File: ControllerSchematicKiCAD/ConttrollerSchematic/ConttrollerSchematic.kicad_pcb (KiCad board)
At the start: 2 copper layers, 175 x 50 mm, 10 parts, among them SW1 SW_Push, SW2 SW_Push

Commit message: Schematic updates
lots of stuff
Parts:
- removed D1, D2, D3, D4: LED, LED_THT:LED_D5.0mm
- removed REF** (x2): PinSocket_1x15_P2.54mm_Vertical, Connector_PinSocket_2.54mm:PinSocket_1x15_P2.54mm_Vertical
- removed REF**: PinSocket_1x05_P2.54mm_Horizontal, Connector_PinSocket_2.54mm:PinSocket_1x05_P2.54mm_Horizontal
- removed REF**: Buzzer_12x9.5RM7.6, Buzzer_Beeper:Buzzer_12x9.5RM7.6
- removed SW1, SW2: SW_Push, Button_Switch_SMD:SW_Push_1P1T-SH_NO_CK_KMR2xxG
- added Button1: SW_Push, Button_Switch_SMD:SW_Push_1P1T-SH_NO_CK_KMR2xxG, F.Cu at (197.6, 136.6)
- added Button2: SW_Push, Button_Switch_SMD:SW_Push_1P1T-SH_NO_CK_KMR2xxG, F.Cu at (188.5, 137.3)
- added Joystick1: Conn_01x05_Socket, Connector_PinSocket_2.54mm:PinSocket_1x05_P2.54mm_Horizontal, F.Cu at (108.8, 129.8)
- added LED1: LED, LED_THT:LED_D5.0mm, F.Cu at (191.6, 121.7)
- added LED2: LED, LED_THT:LED_D5.0mm, F.Cu at (181.1, 121.7)
- added LeftESP1: Conn_01x15_Pin, Connector_PinSocket_2.54mm:PinSocket_1x15_P2.54mm_Vertical, F.Cu at (142.7, 117.8)
- added RightESP1: Conn_01x15_Pin, Connector_PinSocket_2.54mm:PinSocket_1x15_P2.54mm_Vertical, F.Cu at (159.2, 117.7)
- added Screen1: Conn_01x04_Socket, Connector_PinSocket_1.00mm:PinSocket_1x04_P1.00mm_Vertical, F.Cu at (99.0, 120.1)

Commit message: auto routed
heheh
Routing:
- net GND: track 0.00 -> 154.3 mm, vias 0 -> 1
- net Net-(RightESP1-Pin_14): track 0.00 -> 105.5 mm, vias 0 -> 1
- net Net-(RightESP1-Pin_11): track 0.00 -> 86.1 mm, vias 0 -> 1
- net V+: track 0.00 -> 85.6 mm
- net Net-(LeftESP1-Pin_3): track 0.00 -> 76.3 mm, vias 0 -> 1
- net Net-(LED1-A): track 0.00 -> 67.9 mm, vias 0 -> 1
- net Net-(LED2-A): track 0.00 -> 65.2 mm, vias 0 -> 1
- net Net-(LeftESP1-Pin_6): track 0.00 -> 55.2 mm
- net /L8: track 0.00 -> 39.2 mm
- net /Pin L5: track 0.00 -> 34.7 mm
- net /L7: track 0.00 -> 34.7 mm

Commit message: moved something
moved the esp
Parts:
- moved RightESP1 1.78 mm to (161.0, 117.7)
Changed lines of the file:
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@@
 	(footprint "Connector_PinSocket_2.54mm:PinSocket_1x15_P2.54mm_Vertical"
 		(layer "F.Cu")
-		(at 159.22 117.73)
+		(at 161 117.73)
 		(descr "Through hole straight socket strip, 1x15, 2.54mm pitch, single row (from Kicad 4.0.7), script generated")
 		(tags "Through hole socket strip THT 1x15 2.54mm single row")
@@
 	)
 	(segment
-		(start 159.22 117.73)
-		(end 160.3717 117.73)
-		(width 0.2)
-		(layer "F.Cu")
-		(net 1)
-	)
-	(segment
-		(start 164.3517 121.71)
-		(end 181.08 121.71)
+		(start 161 117.73)
+		(end 162.1517 117.73)
+		(width 0.2)
+		(layer "F.Cu")
+		(net 1)
+	)
+	(segment
+		(start 166.1317 121.71)
+		(end 182.86 121.71)
 		(width 0.2)
 		(layer "F.Cu")
@@
 	)
 	(segment
-		(start 142.68 119.525)
-		(end 156.2733 119.525)
+		(start 144.46 119.525)
+		(end 158.0533 119.525)
 		(width 0.2)
 		(layer "F.Cu")
@@
 	)
 	(segment
-		(start 160.3717 117.73)
-		(end 164.3517 121.71)
+		(start 162.1517 117.73)
+		(end 166.1317 121.71)
 		(width 0.2)
 		(layer "F.Cu")
@@
 	)
 	(segment
-		(start 159.22 117.73)
-		(end 158.0683 117.73)
+		(start 161 117.73)
+		(end 159.8483 117.73)
 		(width 0.2)
 		(layer "F.Cu")
@@
 	)
 	(segment
-		(start 156.2733 119.525)
-		(end 158.0683 117.73)
+		(start 158.0533 119.525)
+		(end 159.8483 117.73)
 		(width 0.2)
 		(layer "F.Cu")
@@
 	)
 	(segment
-		(start 157.9825 121.5075)
-		(end 159.22 120.27)
+		(start 159.7625 121.5075)
+		(end 161 120.27)
 		(width 0.2)
 		(layer "F.Cu")
@@
 	)
 	(segment
-		(start 138.2257 121.5075)
-		(end 157.9825 121.5075)
+		(start 140.0057 121.5075)
+		(end 159.7625 121.5075)
 		(width 0.2)
 		(layer "F.Cu")
@@
 	)
 	(segment
-		(start 145.8122 139.2417)
-		(end 192.9666 139.2417)
+		(start 147.5922 139.2417)
+		(end 194.7466 139.2417)
 		(width 0.2)
 		(layer "F.Cu")
@@
 	)
 	(segment
-		(start 165.179 137.3002)
-		(end 159.6971 131.8183)
+		(start 166.959 137.3002)
+		(end 161.4771 131.8183)
 		(width 0.2)
 		(layer "F.Cu")
@@
 	)
 	(segment
-		(start 158.2933 134.24)
-		(end 146.44 134.24)
+		(start 160.0733 134.24)
+		(end 148.22 134.24)
 		(width 0.2)
 		(layer "F.Cu")
@@
 	)
 	(segment
-		(start 158.743 131.8183)
-		(end 158.0683 132.493)
+		(start 160.523 131.8183)
+		(end 159.8483 132.493)
 		(width 0.2)
 		(layer "F.Cu")
@@
 	)
 	(segment
-		(start 158.3413 134.192)
-		(end 158.2933 134.24)
-		(width 0.2)
-		(layer "F.Cu")
-		(net 7)
-	)
-	(segment
-		(start 158.3413 134.192)
-		(end 158.2933 134.24)
-		(width 0.2)
-		(layer "F.Cu")
-		(net 7)
-	)
-	(segment
-		(start 158.0683 133.919)
-		(end 158.3413 134.192)
-		(width 0.2)
-		(layer "F.Cu")
-		(net 7)
-	)
-	(segment
-		(start 159.6971 131.8183)
-		(end 158.743 131.8183)
-		(width 0.2)
-		(layer "F.Cu")
-		(net 7)
-	)
-	(segment
-		(start 158.0683 132.493)
-		(end 158.0683 133.919)
+		(start 160.1213 134.192)
+		(end 160.0733 134.24)
+		(width 0.2)
+		(layer "F.Cu")
+		(net 7)
+	)
+	(segment
+		(start 160.1213 134.192)
+		(end 160.0733 134.24)
+		(width 0.2)
+		(layer "F.Cu")
+		(net 7)
+	)
+	(segment
+		(start 159.8483 133.919)
+		(end 160.1213 134.192)
+		(width 0.2)
+		(layer "F.Cu")
+		(net 7)
+	)
+	(segment
+		(start 161.4771 131.8183)
+		(end 160.523 131.8183)
+		(width 0.2)
+		(layer "F.Cu")
+		(net 7)
+	)
+	(segment
+		(start 159.8483 132.493)
+		(end 159.8483 133.919)
 		(width 0.2)
 		(layer "F.Cu")
@@
 	)
 	(segment
-		(start 145.3716 126.7205)
-		(end 189.1295 126.7205)
+		(start 147.1516 126.7205)
+		(end 190.9095 126.7205)
 		(width 0.2)
 		(layer "F.Cu")
@@
 	)
 	(segment
-		(start 146.5713 124.08)
-		(end 181.25 124.08)
+		(start 148.3513 124.08)
+		(end 183.03 124.08)
 		(width 0.2)
 		(layer "F.Cu")
@@
 	)
 	(segment
-		(start 158 149.53)
-		(end 159.22 150.75)
+		(start 159.78 149.53)
+		(end 161 150.75)
 		(width 0.2)
 		(layer "F.Cu")
@@
 	)
 	(segment
-		(start 102.2056 149.53)
-		(end 158 149.53)
+		(start 103.9856 149.53)
+		(end 159.78 149.53)
 		(width 0.2)
 		(layer "F.Cu")
@@
 	)
 	(segment
-		(start 159.22 143.13)
-		(end 158.0763 141.9863)
+		(start 161 143.13)
+		(end 159.8563 141.9863)
 		(width 0.2)
 		(layer "F.Cu")
@@
 	)
 	(segment
-		(start 158.0763 141.9863)
-		(end 103.5375 141.9863)
-		(width 0.2)
-		(layer "F.Cu")
+		(start 159.8563 141.9863)
+		(end 105.3175 141.9863)
+		(width 0.2)
+		(layer "F.Cu")

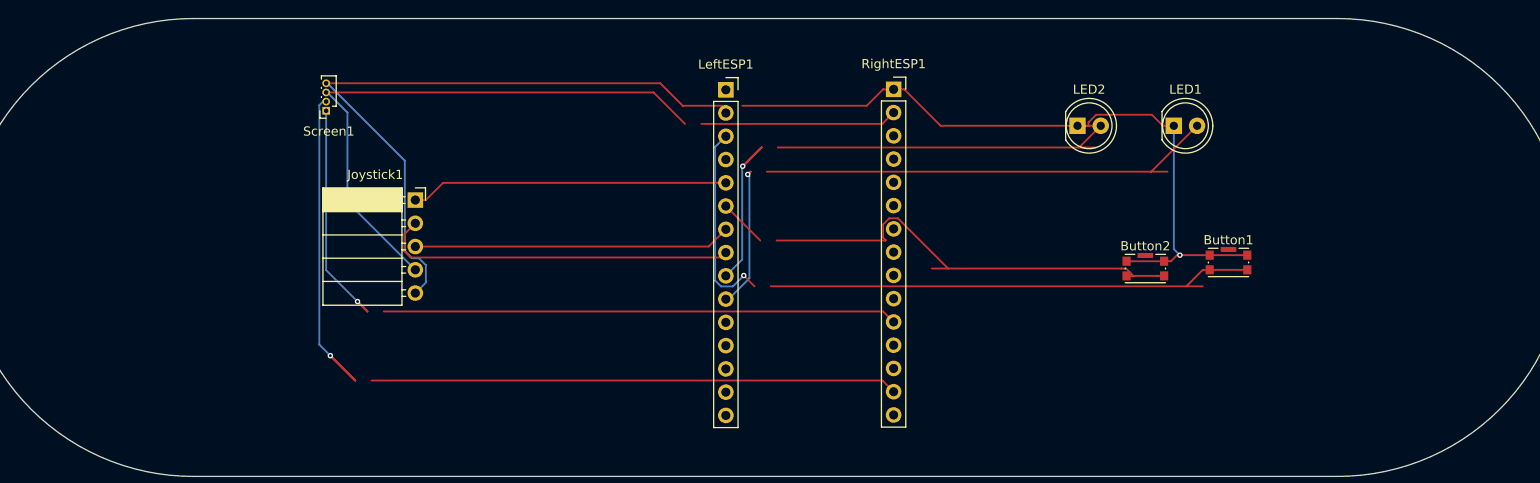
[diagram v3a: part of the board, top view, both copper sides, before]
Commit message: I changed the location of some stuff redo the button size
Changed buttons footprint, delete all wiring for now
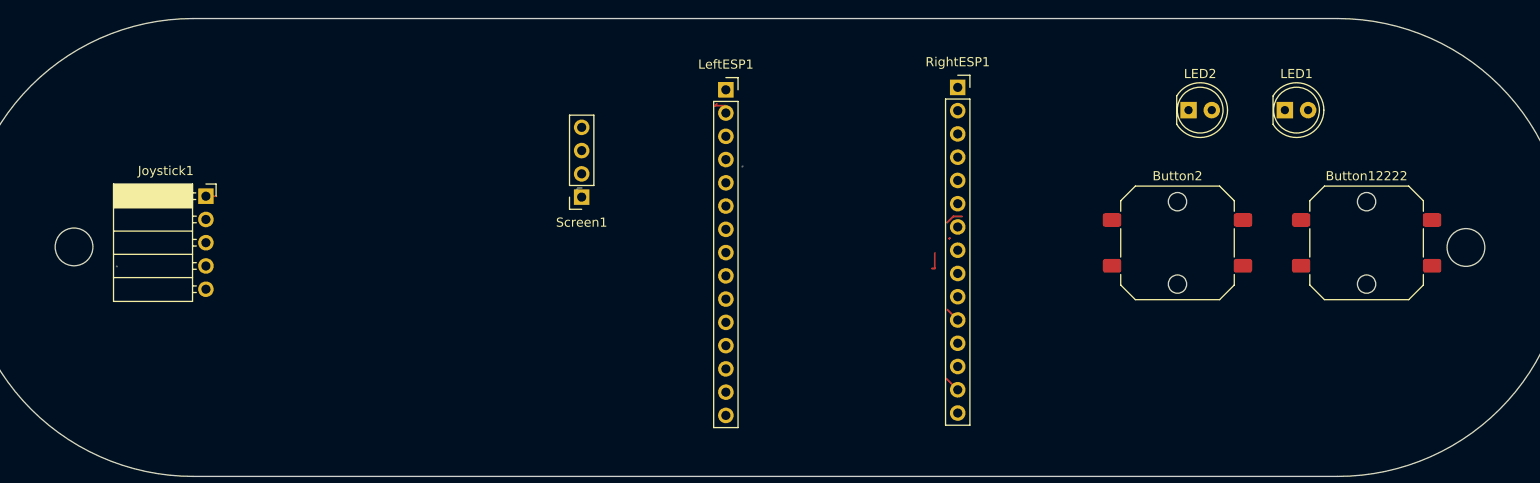
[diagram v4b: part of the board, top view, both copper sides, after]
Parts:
- Button12222: renamed from Button1; footprint Button_Switch_SMD:SW_Push_1P1T-SH_NO_CK_KMR2xxG -> Button_Switch_SMD:SW_Push_1P1T_NO_CK_PTS125Sx73PSMTR
- Button2: footprint Button_Switch_SMD:SW_Push_1P1T-SH_NO_CK_KMR2xxG -> Button_Switch_SMD:SW_Push_1P1T_NO_CK_PTS125Sx73PSMTR
- Screen1: footprint Connector_PinSocket_1.00mm:PinSocket_1x04_P1.00mm_Vertical -> Connector_PinSocket_2.54mm:PinSocket_1x04_P2.54mm_Vertical
- moved Screen1 29.5 mm to (126.9, 129.5)
- moved Joystick1 22.9 mm to (85.9, 129.4)
- moved Button12222 15.2 mm to (212.7, 134.5)
- moved LED1 12.2 mm to (203.7, 120.0)
- moved LED2 12.2 mm to (193.2, 120.0)
- moved RightESP1 7.00 mm to (168.0, 117.5)
- moved Button2 4.49 mm to (192.0, 134.5)
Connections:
- net /Pin L5 renamed /L5
- net Net-(LED1-A) renamed /L10
- net Net-(LED2-A) renamed /L9
- net Net-(LeftESP1-Pin_3) renamed /L3
- net Net-(LeftESP1-Pin_6) renamed /L6
- net Net-(RightESP1-Pin_11) renamed /R14
- net Net-(RightESP1-Pin_14) renamed /R11
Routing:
- net GND: track 154.3 -> 2.27 mm, vias 1 -> 0
- net /R11: track 105.5 -> 1.99 mm, vias 1 -> 0
- net V+: track 85.6 -> 0.00 mm
- net /R14: track 86.1 -> 2.55 mm, vias 1 -> 0
- net /L3: track 76.3 -> 0.00 mm, vias 1 -> 0
- net /L10: track 67.9 -> 0.30 mm, vias 1 -> 0
- net /L9: track 65.2 -> 0.08 mm, vias 1 -> 0
- net /L6: track 55.2 -> 0.00 mm
- net /L8: track 39.2 -> 0.75 mm
- net /L7: track 34.7 -> 0.00 mm
- net /L5: track 34.7 -> 1.15 mm
- net unconnected-(RightESP1-Pin_9-Pad9): track 0.00 -> 4.06 mm
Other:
- outline, holes or cut-outs redrawn

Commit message: changed the dimension
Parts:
- moved LeftESP1 76.1 mm to (141.5, 41.7)
- moved RightESP1 76.1 mm to (166.8, 41.5)
- moved Button2 75.7 mm to (197.8, 59.0)
- moved LED1 75.7 mm to (209.6, 44.5)
- moved LED2 75.7 mm to (199.1, 44.5)
- moved Button12222 75.6 mm to (216.8, 59.0)
- moved Joystick1 75.6 mm to (88.9, 53.9)
- moved Screen1 69.2 mm to (125.0, 60.3)
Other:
- board size 175 x 50 mm -> 174 x 42 mm
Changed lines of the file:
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@@
 	(footprint "Connector_PinSocket_2.54mm:PinSocket_1x05_P2.54mm_Horizontal"
 		(layer "F.Cu")
-		(at 85.9 129.4)
+		(at 88.9 53.9)
 		(descr "Through hole angled socket strip, 1x05, 2.54mm pitch, 8.51mm socket length, single row (from Kicad 4.0.7), script generated")
 		(tags "Through hole angled socket strip THT 1x05 2.54mm single row")
@@
 	(footprint "Connector_PinSocket_2.54mm:PinSocket_1x15_P2.54mm_Vertical"
 		(layer "F.Cu")
-		(at 142.68 117.78)
+		(at 141.5 41.72)
 		(descr "Through hole straight socket strip, 1x15, 2.54mm pitch, single row (from Kicad 4.0.7), script generated")
 		(tags "Through hole socket strip THT 1x15 2.54mm single row")
@@
 	(footprint "LED_THT:LED_D5.0mm"
 		(layer "F.Cu")
-		(at 203.725 120)
+		(at 209.575 44.5)
 		(descr "LED, diameter 5.0mm, 2 pins, http://cdn-reichelt.de/documents/datenblatt/A500/LL-504BC2E-009.pdf, generated by kicad-footprint-generator")
 		(tags "LED")
@@
 	(footprint "Button_Switch_SMD:SW_Push_1P1T_NO_CK_PTS125Sx73PSMTR"
 		(layer "F.Cu")
-		(at 192 134.5)
+		(at 197.85 59)
 		(descr "Tactile switch, 12x12 mm, H7.3 mm, square snap fit actuator, with pegs, gullwing terminals, https://www.ckswitches.com/media/1462/pts125.pdf")
 		(tags "button tactile switch SPST 1P1T C&K")
@@
 	(footprint "Button_Switch_SMD:SW_Push_1P1T_NO_CK_PTS125Sx73PSMTR"
 		(layer "F.Cu")
-		(at 212.65 134.5)
+		(at 216.85 59)
 		(descr "Tactile switch, 12x12 mm, H7.3 mm, square snap fit actuator, with pegs, gullwing terminals, https://www.ckswitches.com/media/1462/pts125.pdf")
 		(tags "button tactile switch SPST 1P1T C&K")
@@
 	(footprint "LED_THT:LED_D5.0mm"
 		(layer "F.Cu")
-		(at 193.205 120)
+		(at 199.055 44.5)
 		(descr "LED, diameter 5.0mm, 2 pins, http://cdn-reichelt.de/documents/datenblatt/A500/LL-504BC2E-009.pdf, generated by kicad-footprint-generator")
 		(tags "LED")
@@
 	(footprint "Connector_PinSocket_2.54mm:PinSocket_1x04_P2.54mm_Vertical"
 		(layer "F.Cu")
-		(at 126.93575 129.5 180)
+		(at 124.975 60.3 180)
 		(descr "Through hole straight socket strip, 1x04, 2.54mm pitch, single row (from Kicad 4.0.7), script generated")
 		(tags "Through hole socket strip THT 1x04 2.54mm single row")
 		(property "Reference" "Screen1"
-			(at 0 -2.77 180)
+			(at 1.18 73.29 180)
 			(layer "F.SilkS")
 			(effects
@@
 	(footprint "Connector_PinSocket_2.54mm:PinSocket_1x15_P2.54mm_Vertical"
 		(layer "F.Cu")
-		(at 168 117.52)
+		(at 166.82 41.46)
 		(descr "Through hole straight socket strip, 1x15, 2.54mm pitch, single row (from Kicad 4.0.7), script generated")
 		(tags "Through hole socket strip THT 1x15 2.54mm single row")
@@
 	)
 	(gr_circle
-		(center 71.5 134.938447)
-		(end 71 136.938447)
+		(center 69.5 59)
+		(end 69 61)
 		(stroke
 			(width 0.05)
@@
 	)
 	(gr_arc
-		(start 84.5 160)
-		(mid 59.5 135)
-		(end 84.5 110)
+		(start 86.49226 79.918734)
+		(mid 63.495832 59.622458)
+		(end 85.25 38)
 		(stroke
 			(width 0.05)
@@
 		(layer "Edge.Cuts")
 	)
-	(gr_circle
-		(center 223.5 135)
-		(end 223 137)
+	(gr_arc
+		(start 216.509235 38)
+		(mid 237.5 58.37728)
+		(end 217.754128 79.963069)
 		(stroke
 			(width 0.05)
 			(type default)
 		)
-		(fill no)
 		(layer "Edge.Cuts")
 	)
-	(gr_line
-		(start 209.5 160)
-		(end 84.5 160)
+	(gr_circle
+		(center 232 58.5)
+		(end 231.5 60.5)
 		(stroke
 			(width 0.05)
 			(type default)
 		)
+		(fill no)
 		(layer "Edge.Cuts")
 	)
-	(gr_arc
-		(start 209.5 110)
-		(mid 234.5 135)
-		(end 209.5 160)
+	(gr_line
+		(start 218 79.918734)
+		(end 86 79.918734)
 		(stroke
 			(width 0.05)
-			(type default)
+			(type solid)
 		)
 		(layer "Edge.Cuts")
 	)
 	(gr_line
-		(start 84.5 110)
-		(end 209.5 110)
+		(start 85.25 38)
+		(end 217.25 38)
 		(stroke
 			(width 0.05)
-			(type default)
+			(type solid)
 		)
 		(layer "Edge.Cuts")
 	)
 	(segment
-		(start 141.71 119.315)
-		(end 141.5 119.525)
+		(start 140.53 43.255)
+		(end 140.32 43.465)
 		(width 0.2)
 		(layer "F.Cu")
@@
 	)
 	(segment
-		(start 142.68 119.525)
-		(end 141.5 119.525)
+		(start 141.5 43.465)
+		(end 140.32 43.465)
 		(width 0.2)
 		(layer "F.Cu")
@@
 	)
 	(segment
-		(start 142.68 120.32)
-		(end 142.68 119.525)
+		(start 141.5 44.26)
+		(end 141.5 43.465)
 		(width 0.2)
 		(layer "F.Cu")
@@
 	)
 	(segment
-		(start 142.1463 136.0937)
-		(end 142.68 135.56)
+		(start 140.9663 60.0337)
+		(end 141.5 59.5)
 		(width 0.2)
 		(layer "F.Cu")
@@
 	)
 	(segment
-		(start 85.9 129.4)
-		(end 87.0517 129.4)
+		(start 88.9 53.9)
+		(end 90.0517 53.9)
 		(width 0.2)
 		(layer "F.Cu")
@@
 	)
 	(segment
-		(start 142.68 140.64)
-		(end 142.9798 140.64)
+		(start 141.5 64.58)
+		(end 141.7998 64.58)
 		(width 0.2)
 		(layer "B.Cu")
@@
 	)
 	(segment
-		(start 144.525 126.1263)
-		(end 144.4688 126.1825)
+		(start 143.345 50.0663)
+		(end 143.2888 50.1225)
 		(width 0.2)
 		(layer "B.Cu")
@@
 	)
 	(segment
-		(start 167.1033 134)
-		(end 167.0733 134.03)
+		(start 165.9233 57.94)
+		(end 165.8933 57.97)
 		(width 0.2)
 		(layer "F.Cu")
@@
 	)
 	(segment
-		(start 165.5 137.3002)
-		(end 165.179 137.3002)
+		(start 164.32 61.2402)
+		(end 163.999 61.2402)
 		(width 0.2)
 		(layer "F.Cu")
@@
 	)
 	(segment
-		(start 167.523 131.6083)
-		(end 166.8483 132.283)
+		(start 166.343 55.5483)
+		(end 165.6683 56.223)
 		(width 0.2)
 		(layer "F.Cu")
@@
 	)
 	(segment
-		(start 165.5 135.6033)
-		(end 165.5 137.3002)
+		(start 164.32 59.5433)
+		(end 164.32 61.2402)
 		(width 0.2)
 		(layer "F.Cu")
@@
 	)
 	(segment
-		(start 167.1213 133.982)
-		(end 167.1033 134)
+		(start 165.9413 57.922)
+		(end 165.9233 57.94)
 		(width 0.2)
 		(layer "F.Cu")
@@
 	)
 	(segment
-		(start 167.1213 133.982)
-		(end 167.0733 134.03)
+		(start 165.9413 57.922)
+		(end 165.8933 57.97)
 		(width 0.2)
 		(layer "F.Cu")
@@
 	)
 	(segment
-		(start 168.4771 131.6083)
-		(end 167.523 131.6083)
+		(start 167.2971 55.5483)
+		(end 166.343 55.5483)
 		(width 0.2)
 		(layer "F.Cu")
@@
 	)
 	(segment
-		(start 126.93575 126.5)
-		(end 127.07595 126.5)
+		(start 124.975 57.3)
+		(end 125.1152 57.3)
 		(width 0.2)
 		(layer "B.Cu")
@@
 	)
 	(segment
-		(start 126.93575 127.5)
-		(end 127.06425 127.5)
+		(start 124.975 58.3)
+		(end 125.1035 58.3)
 		(width 0.2)
 		(layer "B.Cu")
@@
 	)
 	(segment
-		(start 168 142.92)
-		(end 166.8563 141.7763)
+		(start 166.82 66.86)
+		(end 165.6763 65.7163)
 		(width 0.2)
 		(layer "F.Cu")
@@
 		(width 0.2)
 		(layer "B.Cu")
-		(net 29)
-	)
-	(segment
-		(start 76.1812 137.08)
-		(end 76.16 137.0588)
-		(width 0.2)
-		(layer "B.Cu")

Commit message: something more
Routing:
- net unconnected-(RightESP1-Pin_9-Pad9): track 4.06 -> 0.00 mm
- net /R14: track 2.52 -> 0.00 mm
- net GND: track 2.27 -> 0.00 mm
- net /R11: track 1.99 -> 0.00 mm
- net /L5: track 1.15 -> 0.00 mm
- net /L8: track 0.75 -> 0.00 mm
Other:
- outline, holes or cut-outs redrawn
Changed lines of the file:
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@@
 			(at 1.18 73.29 180)
 			(layer "F.SilkS")
+			(hide yes)
 			(effects
 				(font
@@
 		(layer "Edge.Cuts")
 	)
+	(gr_line
+		(start 85.999997 79.959574)
+		(end 86 79.918734)
+		(stroke
+			(width 0.05)
+			(type default)
+		)
+		(layer "Edge.Cuts")
+	)
 	(gr_arc
-		(start 86.49226 79.918734)
-		(mid 63.495832 59.622458)
-		(end 85.25 38)
+		(start 86 79.959574)
+		(mid 63.490176 59.375542)
+		(end 85.249993 38.000208)
 		(stroke
 			(width 0.05)
@@
 	)
 	(gr_arc
-		(start 216.509235 38)
-		(mid 237.5 58.37728)
-		(end 217.754128 79.963069)
+		(start 217.25 38)
+		(mid 237.518909 58.623)
+		(end 218.002934 79.959904)
 		(stroke
 			(width 0.05)
@@
 		(layer "Edge.Cuts")
 	)
-	(segment
-		(start 140.53 43.255)
-		(end 140.32 43.465)
-		(width 0.2)
-		(layer "F.Cu")
-		(net 1)
-	)
-	(segment
-		(start 141.5 43.465)
-		(end 140.32 43.465)
-		(width 0.2)
-		(layer "F.Cu")
-		(net 1)
-	)
-	(segment
-		(start 141.5 44.26)
-		(end 141.5 43.465)
-		(width 0.2)
-		(layer "F.Cu")
-		(net 1)
-	)
-	(segment
-		(start 140.9663 60.0337)
-		(end 141.5 59.5)
-		(width 0.2)
-		(layer "F.Cu")
-		(net 5)
-	)
-	(segment
-		(start 88.9 53.9)
-		(end 90.0517 53.9)
-		(width 0.2)
-		(layer "F.Cu")
-		(net 7)
-	)
-	(segment
-		(start 141.5 64.58)
-		(end 141.7998 64.58)
-		(width 0.2)
-		(layer "B.Cu")
-		(net 8)
-	)
-	(segment
-		(start 143.345 50.0663)
-		(end 143.2888 50.1225)
-		(width 0.2)
-		(layer "B.Cu")
-		(net 9)
-	)
-	(segment
-		(start 165.9233 57.94)
-		(end 165.8933 57.97)
-		(width 0.2)
-		(layer "F.Cu")
-		(net 23)
-	)
-	(segment
-		(start 164.32 61.2402)
-		(end 163.999 61.2402)
-		(width 0.2)
-		(layer "F.Cu")
-		(net 23)
-	)
-	(segment
-		(start 166.343 55.5483)
-		(end 165.6683 56.223)
-		(width 0.2)
-		(layer "F.Cu")
-		(net 23)
-	)
-	(segment
-		(start 164.32 59.5433)
-		(end 164.32 61.2402)
-		(width 0.2)
-		(layer "F.Cu")
-		(net 23)
-	)
-	(segment
-		(start 165.9413 57.922)
-		(end 165.9233 57.94)
-		(width 0.2)
-		(layer "F.Cu")
-		(net 23)
-	)
-	(segment
-		(start 165.9413 57.922)
-		(end 165.8933 57.97)
-		(width 0.2)
-		(layer "F.Cu")
-		(net 23)
-	)
-	(segment
-		(start 167.2971 55.5483)
-		(end 166.343 55.5483)
-		(width 0.2)
-		(layer "F.Cu")
-		(net 23)
-	)
-	(segment
-		(start 168 150.54)
-		(end 166.78 149.32)
-		(width 0.2)
-		(layer "F.Cu")
-		(net 28)
-	)
-	(segment
-		(start 124.975 57.3)
-		(end 125.1152 57.3)
-		(width 0.2)
-		(layer "B.Cu")
-		(net 28)
-	)
-	(segment
-		(start 124.975 58.3)
-		(end 125.1035 58.3)
-		(width 0.2)
-		(layer "B.Cu")
-		(net 28)
-	)
-	(segment
-		(start 166.82 66.86)
-		(end 165.6763 65.7163)
-		(width 0.2)
-		(layer "F.Cu")
-		(net 29)
-	)
-	(segment
-		(start 126.93575 128.5)
-		(end 126.57955 128.5)
-		(width 0.2)
-		(layer "B.Cu")
-		(net 29)
-	)
-	(segment
-		(start 126.57955 128.5)
-		(end 126.19035 128.8892)
-		(width 0.2)
-		(layer "B.Cu")
-		(net 29)
+	(gr_line
+		(start 218.002935 79.959904)
+		(end 218.002934 79.918734)
+		(stroke
+			(width 0.05)
+			(type default)
+		)
+		(layer "Edge.Cuts")
 	)
 	(group ""
